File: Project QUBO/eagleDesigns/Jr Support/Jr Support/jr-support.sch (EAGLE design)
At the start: 195 parts, among them U1 PCA9685, U2 BME280

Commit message: 
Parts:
- removed 2PIN_2: 12V reg switch, molex:KK254_VERT_2PIN22-29-2021
- removed C64: (no value), resistor:C-USC0805
- removed C65, C80, C81: 22u, resistor:C-USC0805
- removed C66, C67: 2.2u, resistor:C-USC0805
- removed C69: 1u, resistor:C-USC0805
- removed C70, C76, C77, C78, C79, C82, C83: 0.1u, resistor:C-USC0805
- removed C71, C74, C75: 1n, resistor:C-USC0805
- removed C72, C73: 47n, resistor:C-USC0805
- removed C84: 100u,<50mO, resistor:C-USC0805
- removed D1: (no value), diode:DIODE-SOD123
- removed JP2, JP3: SUPERSABRE_2CIRCUIT, molex:SUPERSABRE_2CIRCUIT
- removed R26: 10\, resistor:R-US_R0805
- removed R27: 200k, resistor:R-US_R0805
- removed R28: 8.2k, resistor:R-US_R0805
- removed R29, R34: 100m, resistor:R-US_R0805
- removed R30, R31: ~50k, resistor:R-US_R0805
- removed R32: 10k, resistor:R-US_R0805
- removed R33, R35, R36: 22m, resistor:R-US_R0805
- added 2PIN_5: (no value), molex:KK254_VERT_2PIN22-29-2021
- added C33: 0.1u, resistor:C-USC0805
- added R13: 0, resistor:R-US_R0805
- added U$41, U$59: VTVS, diode:VTVS
- added U$42, U$43, U$44: ADC121C021, texas:ADC121C021
- added U$45: 74LVC1G14, NXP:74LVC1G14
- added U$57: NCP1117, ONSemi:NCP1117
- 2PIN_3: value Relay switch -> (none)
- C10, C16: value 47n -> (none)
- C13, C21, C7: value 0.1u -> (none)
- C14, C22, C8: value 47n -> 0.1u
- C15, C9: value 0.1u -> 47n
- C29: value 100u -> 47n; device resistor:CPOL-USE3.5-8 -> resistor:C-USC0805
- C30: value 100u -> (none); device resistor:CPOL-USE3.5-8 -> resistor:C-USC0805
- C32, C60: value (none) -> 1u
- C34, C61: value (none) -> 10u
- C37: value 10u -> 47n
- C56: value (none) -> 0.1u
- C57: value (none) -> 47n
- C59: value (none) -> 100u; device resistor:C-USC0805 -> resistor:CPOL-USE3.5-8
- C63: value 0.1u -> 10u
- JP1: value SUPERSABRE_2CIRCUIT -> 2_SUPERSABRE; device molex:SUPERSABRE_2CIRCUIT -> molex:2_SUPERSABRE
- R18: value 10k -> 510
- R20, R22: value 10k -> 0
- R21: value 12k -> 6.8k
- R23: value 51k -> 510
- R24: value 5.1k -> 6.8k
- R25: value 5m -> 100
- U$10, U$16: value 4A Fuse -> VTVS; device littelfuse:154-OMNI_BLOK -> diode:VTVS
- U$13, U$22: value ACS713SOIC -> VTVS; device allegro:ACS713SOIC -> diode:VTVS
- U$14, U$23, U$8: value 4A Fuse -> ACS713SOIC; device littelfuse:154-OMNI_BLOK -> allegro:ACS713SOIC
- U$15, U$9: value ACS713SOIC -> 4A Fuse; device allegro:ACS713SOIC -> littelfuse:154-OMNI_BLOK
- U$26: value 24V -> VTVS; device ONSemi:2-PIN_TVS_SOD-323 -> diode:VTVS
- U$27: value LTC4364MSOP -> 4A Fuse; device linear:LTC4364MSOP -> littelfuse:154-OMNI_BLOK
- U$28, U$32, U$34: value (none) -> VTVS; device fairchild:FDMC8360LET40PWR33 -> diode:VTVS
- U$29: value 24V -> ACS713SOIC; device diode:2-PIN_TVS_SOD-323 -> allegro:ACS713SOIC
- U$30, U$31, U$58: value 24V -> VTVS; device diode:2-PIN_TVS_SOD-323 -> diode:VTVS
- U$33: value MAX1737 -> VTVS; device maxim:MAX1737 -> diode:VTVS
- U$37: value (none) -> 4A Fuse; device fairchild:FDMC8360LET40PWR33 -> littelfuse:154-OMNI_BLOK
- U$38: value (none) -> VTVS; device resistor:DUAL-L -> diode:VTVS
- U$39: value SBR2065 -> ACS713SOIC; device diode:SBR2065 -> allegro:ACS713SOIC
- U$40: value NTCLE201E3 -> 4A Fuse; device vishay:NTCLE201E3 -> littelfuse:154-OMNI_BLOK
- U$46: value 5V -> ESD9X3; device ONSemi:2-PIN_TVS_SOD-323 -> diode:ESD9X3
- U$47: value 24V -> ESD9X3; device ONSemi:2-PIN_TVS_SOD-323 -> diode:ESD9X3
- U$48, U$49: value 12V -> ESD9X3; device ONSemi:2-PIN_TVS_SOD-323 -> diode:ESD9X3
- U$50: value 5V -> VTVS; device ONSemi:2-PIN_TVS_SOD-923 -> diode:VTVS
- U$51: value 3V3 -> DESD; device ONSemi:2-PIN_TVS_SOD-923 -> diode:DESD
- U$52, U$54: value 5V -> DESD; device ONSemi:2-PIN_TVS_SOD-923 -> diode:DESD
- U$53: value 12V -> DESD; device ONSemi:2-PIN_TVS_SOD-323 -> diode:DESD
- U$55: value 24V -> NCP1117; device diode:2-PIN_TVS_SOD-323 -> ONSemi:NCP1117
- U$56: value 24V -> 74LVC1G14; device diode:2-PIN_TVS_SOD-323 -> NXP:74LVC1G14
- U$7: value ACS713SOIC -> ADS7828; device allegro:ACS713SOIC -> texas:ADS7828
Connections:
- removed net N$18 (its old number): C10.1, U$9.FILTER
- removed net N$20 (its old number): U$10.P$1, U$9.IP-
- removed net N$25 (its old number): 4PIN_5.P$4, C58.1, U$14.P$2
- removed net N$27 (its old number): C16.1, U$15.FILTER
- removed net N$64: C70.1, R32.1
- removed net N$65: C66.1, C67.1, U$33.!SHDN!, U$33.CELL, U$33.VL
- removed net N$67: C71.1, R32.2, U$33.CCV
- removed net N$68: C69.1, R30.1, U$33.ISETIN, U$33.ISETOUT, U$33.REF
- removed net N$69: C72.1, U$33.CCI
- removed net N$70: C73.1, U$33.CCS
- removed net N$71: C74.1, U$33.TIMER1
- removed net N$72: C75.1, U$33.TIMER2
- removed net N$73: C76.1, R33.2, R35.2, R36.2, U$33.CSSP
- removed net N$74: C77.1, C80.1, C81.1, R33.1, R35.1, R36.1, U$33.CSSN, U$34.DRAIN
- removed net N$75: C78.1, U$33.LX
- removed net N$76: C78.2, D1.C, U$33.BST
- removed net N$77: C82.1, R29.2, R34.2, U$33.CS, U$38.P$3
- removed net N$79: U$33.DLO, U$37.GATE
- removed net N$80: U$33.DHI, U$34.GATE
- removed net N$81: U$34.SOURCE, U$37.DRAIN, U$38.P$1
- removed net N$82: U$33.PGND, U$37.SOURCE
- removed net N$83: C79.1, D1.A, U$33.VLO
- removed net N$84: U$33.THM, U$40.1
- removed net V_BATT: 2PIN_3.P$1, C65.1, R25.2, R28.2, U$27.OUT
- removed net V_BATT2: C29.+, C37.1, JP2.P$2, U$30.P$2
- removed net V_SHORE: C30.+, C62.1, JP3.P$2, U$29.P$2, U$39.A
- new net N$21: C15.1, U$14.FILTER
- new net N$23: R22.1, U$7.COM
- new net N$30: U$23.IP-, U$27.P$1
- new net N$49: C60.1, R23.2, U$56.IN
- new net T1_CURR: U$4.VIOUT, U$7.CH0
- new net T2_CURR: U$7.CH1, U$8.VIOUT
- new net T3_CURR: U$11.VIOUT, U$7.CH2
- new net T4_CURR: U$14.VIOUT, U$7.CH3
- new net T5_CURR: U$17.VIOUT, U$7.CH4
- new net T6_CURR: U$23.VIOUT, U$7.CH5
- new net T7_CURR: U$29.VIOUT, U$7.CH6
- new net T8_CURR: U$39.VIOUT, U$7.CH7
- net 12V: now also U$46.C, U$47.C, U$48.C, U$49.C; no longer U$48.P$2, U$49.P$2
- net 3V3: now also U2.SDO/ADR; no longer U$51.P$2
- net 5V: now also C14.1, C22.1, C33.1, C56.1, C8.1, R21.2, U$14.VCC, U$23.VCC, U$29.VCC, U$39.VCC, U$42.ADR1, U$42.VDD, U$43.ADR0, U$43.ADR1, U$43.VDD, U$44.VDD, U$45.VDD, U$51.C, U$52.C, U$53.C, U$54.C, U$7.REF, U$7.VDD, U$8.VCC; no longer 2PIN_2.P$1, C13.1, C15.1, C21.1, C9.1, U$13.VCC, U$15.VCC, U$22.VCC, U$46.P$2, U$50.P$2, U$52.P$2, U$7.VCC, U$9.VCC
- net AIN0: no longer U$19.VIOUT
- net AIN1: no longer U$2.VIOUT, U$35.VIOUT
- net AIN10: no longer U$17.VIOUT
- net AIN11: no longer U$22.VIOUT
- net AIN2: no longer U$4.VIOUT
- net AIN3: no longer U$7.VIOUT
- net AIN4: no longer U$9.VIOUT
- net AIN5: no longer U$11.VIOUT
- net AIN8: no longer U$13.VIOUT
- net AIN9: no longer U$15.VIOUT
- net CPU_ON: now also U$45.OUT; no longer 2PIN_2.P$2, C34.1, U$55.P$2
- net GND: now also C29.2, C30.2, C33.2, C59.-, R13.1, R22.2, U$10.A, U$13.A, U$14.GND, U$16.A, U$22.A, U$23.GND, U$26.A, U$28.A, U$29.GND, U$30.A, U$31.A, U$32.A, U$33.A, U$34.A, U$38.A, U$39.GND, U$41.A, U$42.ADR0, U$42.GND, U$43.GND, U$44.ADR0, U$44.ADR1, U$44.GND, U$46.A, U$47.A, U$48.A, U$49.A, U$50.A, U$51.A, U$52.A, U$53.A, U$54.A, U$55.GND, U$57.GND, U$7.A0, U$7.A1, U$8.GND; no longer C29.-, C30.-, C32.2, C59.2, C60.2, C64.2, C65.2, C66.2, C67.2, C69.2, C70.2, C71.2, C72.2, C73.2, C74.2, C75.2, C76.2, C77.2, C79.2, C80.2, C81.2, C82.2, C83.2, C84.2, JP2.P$1, JP3.P$1, R18.1, R22.1, R24.1, R31.1, U$13.GND, U$15.GND, U$22.GND, U$26.P$1, U$27.GND, U$29.P$1, U$30.P$1, U$31.P$1, U$33.GND, U$40.2, U$46.P$1, U$47.P$1, U$48.P$1, U$49.P$1, U$50.P$1, U$51.P$1, U$52.P$1, U$53.P$1, U$54.P$1, U$55.P$1, U$56.P$1, U$58.P$1, U$9.GND, U2.SDO/ADR
- net N$12: now also C9.1, U$8.FILTER; no longer C8.1, U$7.FILTER
- net N$14: now also U$31.C
- net N$16: now also C10.1, U$30.C, U$9.P$2; no longer C55.1, U$8.P$2
- net N$17: now also U$8.IP-, U$9.P$1; no longer U$7.IP-, U$8.P$1
- net N$19: now also C13.1, U$12.P$2, U$26.C; no longer C57.1, U$10.P$2
- net N$22: now also C16.1, U$15.P$2, U$28.C; no longer C56.1, U$12.P$2
- net N$24: now also U$14.IP-, U$15.P$1; no longer C14.1, U$13.FILTER
- net N$26: now also 4PIN_5.P$4, C21.1, U$18.P$2; no longer U$13.IP-, U$14.P$1
- net N$28: now also C29.1, U$23.FILTER; no longer 4PIN_6.P$4, C59.1, U$16.P$2
- net N$29: now also 4PIN_6.P$4, C30.1, U$13.C, U$27.P$2; no longer U$15.IP-, U$16.P$1
- net N$31: now also C37.1, U$29.FILTER; no longer 4PIN_7.P$4, C61.1, U$18.P$2
- net N$36: now also 4PIN_7.P$4, C55.1, U$16.C, U$37.P$2; no longer C22.1, U$22.FILTER
- net N$37: now also U$29.IP-, U$37.P$1; no longer R26.1, U$27.HGATE
- net N$38: now also C57.1, U$39.FILTER; no longer 4PIN_10.P$4, C60.1, U$23.P$2
- net N$39: now also 4PIN_10.P$4, C58.1, U$10.C, U$40.P$2; no longer R20.1, R21.2, U$27.UV
- net N$47: now also U$39.IP-, U$40.P$1; no longer R21.1, R22.2, U$27.OV
- net N$48: now also 2PIN_5.P$2, C60.2, U$56.GND, U$58.A; no longer U$22.IP-, U$23.P$1
- net N$50: now also 2PIN_5.P$1, R24.1, U$58.C; no longer R24.2, U$27.FB
- net N$51: now also 2PIN_3.P$2, C32.2, U$45.GND, U$59.A; no longer R20.2, R27.1
- net N$53: now also U$43.VIN; no longer C64.1, U$27.TMR
- net N$54: now also C62.1, R24.2, U$56.VDD, U$57.VOUT; no longer U$27.SOURCE, U$28.SOURCE, U$32.SOURCE
- net N$57: now also U$2.VIOUT, U$42.VIN; no longer R23.2, R28.1
- net N$58: no longer U$53.P$2
- net N$59: now also C32.1, R18.2, U$45.IN; no longer R26.2, U$28.GATE
- net N$60: now also U$44.VIN; no longer R25.1, U$27.SENSE, U$32.DRAIN
- net N$61: now also 2PIN_3.P$1, R18.1, R21.1, U$59.C; no longer U$27.DGATE, U$32.GATE
- net N$62: now also C63.1, R25.1, U$55.VOUT; no longer R30.2, R31.2, U$33.VADJ
- net N$63: now also R25.2, U$1.!INHIBIT!; no longer C63.1, U$33.DCIN, U$39.C
- net N$8: no longer U$54.P$2
- net RELAY-BATT: now also R20.2
- net RELAY-SHORE: now also R13.2
- net RELAY_CTRL: now also U$56.OUT; no longer 2PIN_3.P$2, C32.1, R18.2, U$56.P$2
- net RELAY_OUT: now also C34.1, C59.+, U$50.C, U$55.VIN; no longer U$58.P$2
- net SCL1: now also U$42.SCL, U$43.SCL, U$44.SCL, U$7.SCL
- net SDA1: now also U$42.SDA, U$43.SDA, U$44.SDA, U$7.SDA
- net V_BATT1: now also C61.1, R20.1, U$41.C, U$57.VIN; no longer C83.1, C84.1, R27.2, R29.1, R34.1, U$27.!SHDN!, U$27.VCC, U$28.DRAIN, U$31.P$2, U$33.BATT
- net V_THRUST: now also U$14.IP+, U$23.IP+, U$29.IP+, U$32.C, U$33.C, U$34.C, U$38.C, U$39.IP+, U$8.IP+; no longer U$13.IP+, U$15.IP+, U$22.IP+, U$26.P$2, U$47.P$2, U$7.IP+, U$9.IP+
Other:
- note added: "Address: 1001000 (Thrust ADC)"
- note added: "Address: 1010101 (12V ADC)"
- note added: "Address: 1011001 (5V ADC)"
- note added: "Address: 1011010 (VIN ADC)"
- note added: "Address: 1110111 (0x77) )(BAR30)"
- note added: "Address: 1110111 (0x77)(BME)"
- moved on the sheet: 2PIN_3, 4PIN_10, 4PIN_2, 4PIN_3, 4PIN_4, 4PIN_5, 4PIN_6, 4PIN_7, 5V_REG, C10, C11, C12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

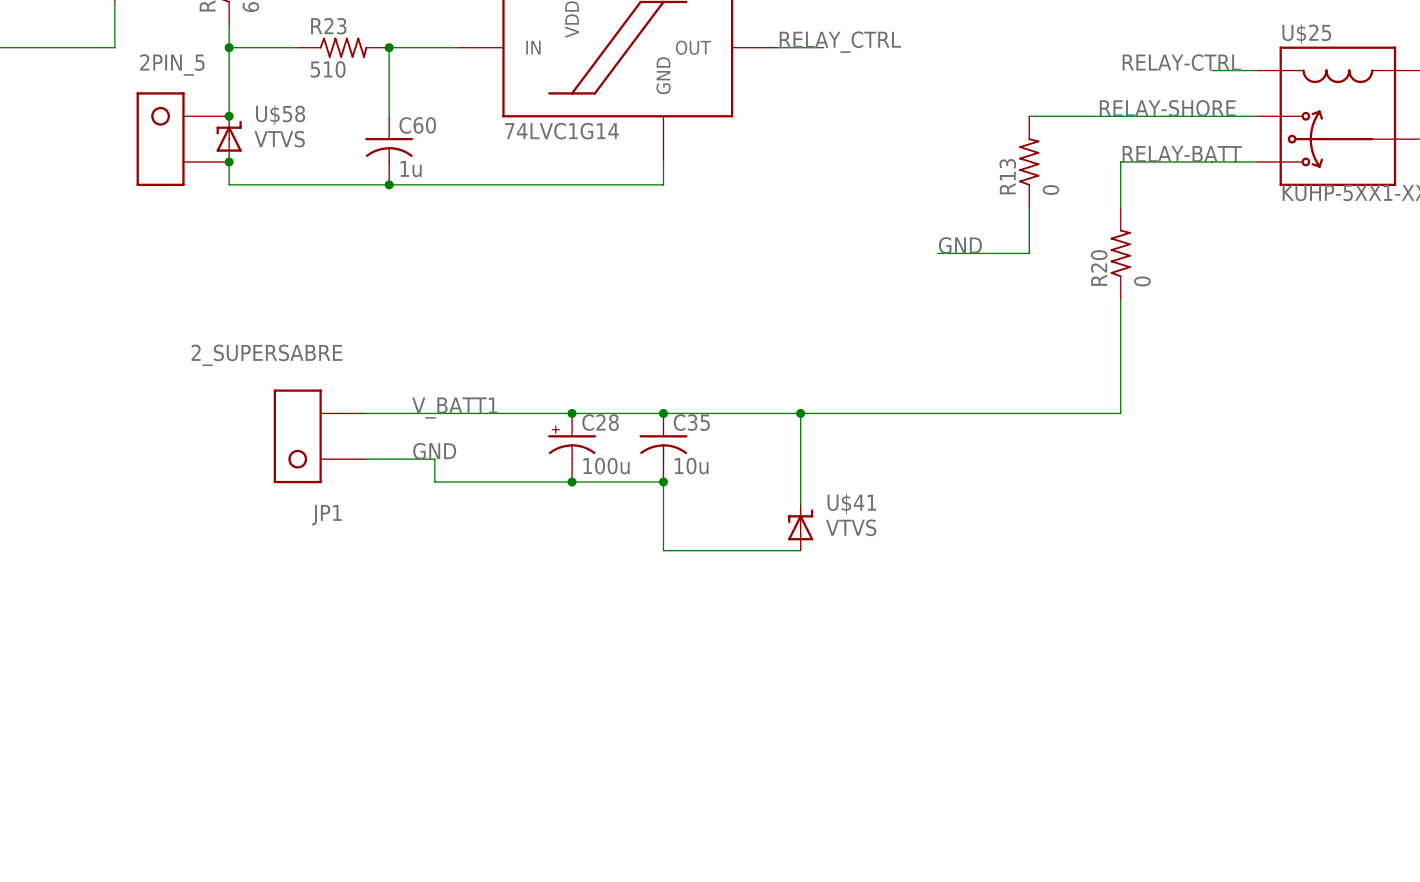
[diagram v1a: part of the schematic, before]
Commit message: 
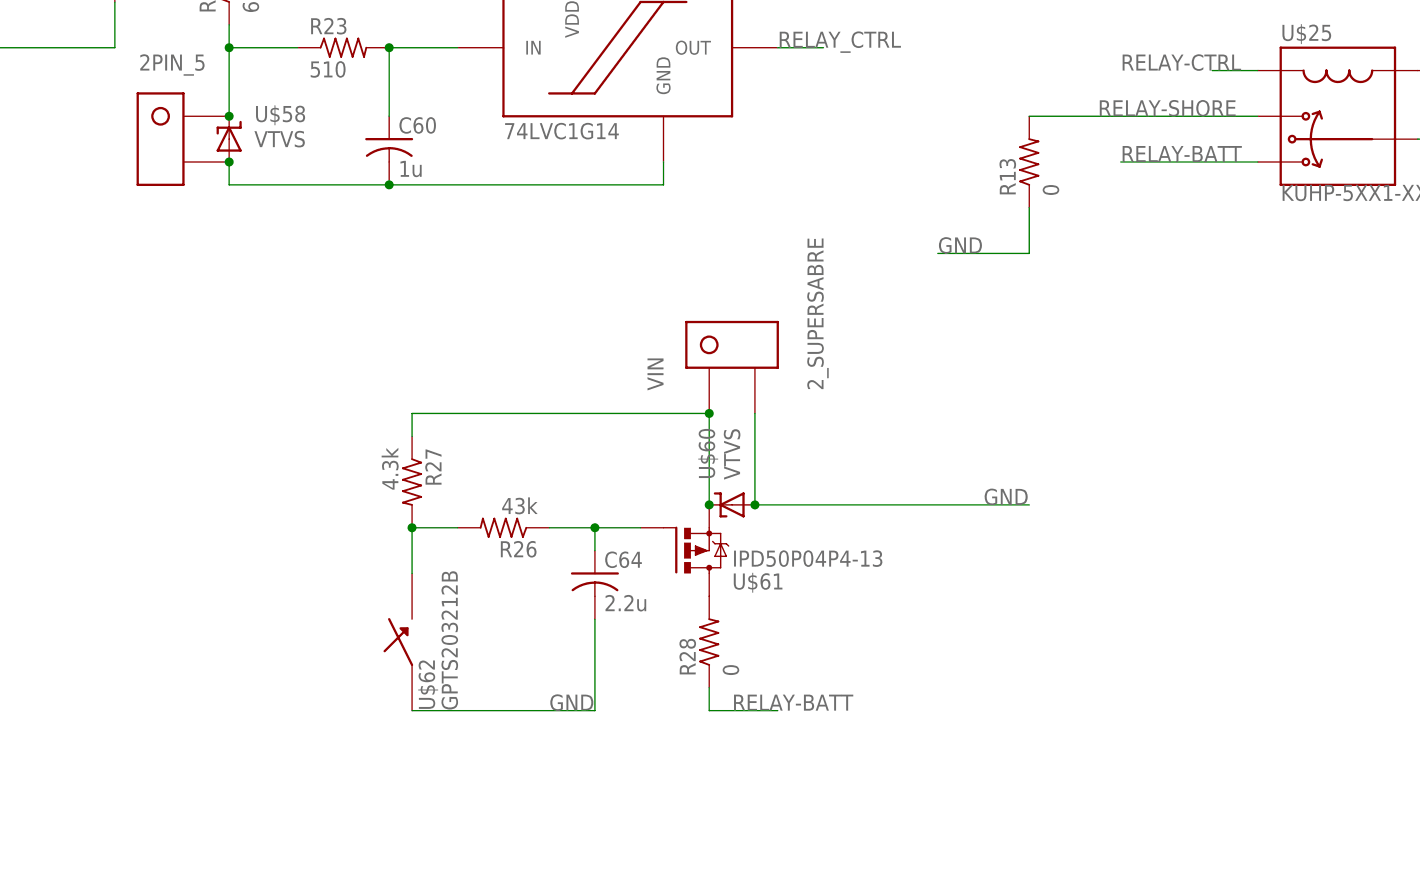
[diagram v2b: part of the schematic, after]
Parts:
- removed C28: 100u, resistor:CPOL-USE3.5-8
- removed C35: 10u, resistor:C-USC0805
- removed JP1: 2_SUPERSABRE, molex:2_SUPERSABRE
- removed R20: 0, resistor:R-US_R0805
- removed U$41: VTVS, diode:VTVS
- added C64: 2.2u, resistor:C-USC0805
- added R26: 43k, resistor:R-US_R0805
- added R27: 4.3k, resistor:R-US_R0805
- added R28: 0, resistor:R-US_R0805
- added U$60: VTVS, diode:VTVS
- added U$61: IPD50P04P4-13, transistor-power:IPD50P04P4-13
- added U$62: GPTS203212B, switches:GPTS203212B
- added VIN: 2_SUPERSABRE, molex:2_SUPERSABRE
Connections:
- new net N$64: R27.1, U$60.C, U$61.D, VIN.P$1
- new net N$65: C64.1, R26.1, U$61.G
- new net N$66: R26.2, R27.2, U$62.P$2
- new net N$67: R28.2, U$61.S
- net GND: now also C64.2, U$60.A, U$62.P$1, VIN.P$2; no longer C28.-, C35.2, JP1.P$1, U$41.A
- net RELAY-BATT: now also R28.1; no longer R20.2
- net V_BATT1: no longer C28.+, C35.1, JP1.P$2, R20.1, U$41.C
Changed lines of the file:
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@@
 <part name="U$1" library="texas" deviceset="PTN78060W" device=""/>
 <part name="U$2" library="allegro" deviceset="ACS713" device="SOIC"/>
-<part name="JP1" library="molex" deviceset="2_SUPERSABRE" device=""/>
 <part name="C2" library="resistor" deviceset="C-US" device="C0805" value="0.1u"/>
 <part name="C3" library="resistor" deviceset="C-US" device="C0805" value="47n"/>
@@
 <part name="R19" library="resistor" deviceset="R-US_" device="R0805" value="10k"/>
 <part name="C27" library="resistor" deviceset="CPOL-US" device="E3.5-8" value="100u"/>
-<part name="C28" library="resistor" deviceset="CPOL-US" device="E3.5-8" value="100u"/>
-<part name="C35" library="resistor" deviceset="C-US" device="C0805" value="10u"/>
 <part name="R13" library="resistor" deviceset="R-US_" device="R0805" value="0"/>
-<part name="R20" library="resistor" deviceset="R-US_" device="R0805" value="0"/>
 <part name="U$7" library="texas" deviceset="ADS7828" device=""/>
 <part name="R22" library="resistor" deviceset="R-US_" device="R0805" value="0"/>
@@
 <part name="U$34" library="diode" deviceset="VTVS" device=""/>
 <part name="U$38" library="diode" deviceset="VTVS" device=""/>
-<part name="U$41" library="diode" deviceset="VTVS" device=""/>
 <part name="U$46" library="diode" deviceset="ESD9X3" device=""/>
 <part name="U$47" library="diode" deviceset="ESD9X3" device=""/>
@@
 <part name="C63" library="resistor" deviceset="C-US" device="C0805" value="10u"/>
 <part name="R25" library="resistor" deviceset="R-US_" device="R0805" value="100"/>
+<part name="VIN" library="molex" deviceset="2_SUPERSABRE" device=""/>
+<part name="U$60" library="diode" deviceset="VTVS" device=""/>
+<part name="U$61" library="transistor-power" deviceset="IPD50P04P4-13" device=""/>
+<part name="R26" library="resistor" deviceset="R-US_" device="R0805" value="43k"/>
+<part name="C64" library="resistor" deviceset="C-US" device="C0805" value="2.2u"/>
+<part name="U$62" library="switches" deviceset="GPTS203212B" device=""/>
+<part name="R27" library="resistor" deviceset="R-US_" device="R0805" value="4.3k"/>
+<part name="R28" library="resistor" deviceset="R-US_" device="R0805" value="0"/>
 </parts>
 <sheets>
@@
 <instance part="U$1" gate="G$1" x="-152.4" y="-7.62"/>
 <instance part="U$2" gate="G$1" x="-66.04" y="-7.62"/>
-<instance part="JP1" gate="G$1" x="-388.62" y="40.64" rot="R180"/>
 <instance part="C2" gate="G$1" x="-45.72" y="5.08"/>
 <instance part="C3" gate="G$1" x="-35.56" y="-12.7"/>
@@
 <instance part="R19" gate="G$1" x="-259.08" y="81.28"/>
 <instance part="C27" gate="G$1" x="-127" y="144.78"/>
-<instance part="C28" gate="G$1" x="-358.14" y="40.64"/>
-<instance part="C35" gate="G$1" x="-347.98" y="40.64"/>
 <instance part="R13" gate="G$1" x="-307.34" y="71.12" rot="R90"/>
-<instance part="R20" gate="G$1" x="-297.18" y="60.96" rot="R90"/>
 <instance part="U$7" gate="G$1" x="58.42" y="-40.64"/>
 <instance part="R22" gate="G$1" x="45.72" y="-60.96" rot="R270"/>
@@
 <instance part="U$34" gate="G$1" x="73.66" y="261.62"/>
 <instance part="U$38" gate="G$1" x="-60.96" y="33.02"/>
-<instance part="U$41" gate="G$1" x="-332.74" y="30.48"/>
 <instance part="U$46" gate="G$1" x="304.8" y="193.04"/>
 <instance part="U$47" gate="G$1" x="284.48" y="203.2"/>
@@
 <instance part="C63" gate="G$1" x="-203.2" y="-25.4"/>
 <instance part="R25" gate="G$1" x="-185.42" y="-22.86"/>
+<instance part="VIN" gate="G$1" x="-340.36" y="50.8" rot="R90"/>
+<instance part="U$60" gate="G$1" x="-340.36" y="33.02" rot="R90"/>
+<instance part="U$61" gate="G$1" x="-345.44" y="27.94" rot="MR180"/>
+<instance part="R26" gate="G$1" x="-365.76" y="30.48" rot="R180"/>
+<instance part="C64" gate="G$1" x="-355.6" y="25.4"/>
+<instance part="U$62" gate="G$1" x="-375.92" y="17.78" rot="R90"/>
+<instance part="R27" gate="G$1" x="-375.92" y="35.56" rot="R270"/>
+<instance part="R28" gate="G$1" x="-342.9" y="17.78" rot="R90"/>
 </instances>
 <busses>
@@
 <wire x1="-167.64" y1="0" x2="-175.26" y2="0" width="0.1524" layer="91"/>
 <label x="-175.26" y="0" size="1.778" layer="95"/>
-</segment>
-<segment>
-<pinref part="JP1" gate="G$1" pin="P$1"/>
-<wire x1="-381" y1="38.1" x2="-373.38" y2="38.1" width="0.1524" layer="91"/>
-<label x="-375.92" y="38.1" size="1.778" layer="95"/>
-<pinref part="C28" gate="G$1" pin="-"/>
-<wire x1="-358.14" y1="35.56" x2="-373.38" y2="35.56" width="0.1524" layer="91"/>
-<wire x1="-373.38" y1="35.56" x2="-373.38" y2="38.1" width="0.1524" layer="91"/>
-<pinref part="C35" gate="G$1" pin="2"/>
-<wire x1="-347.98" y1="35.56" x2="-358.14" y2="35.56" width="0.1524" layer="91"/>
-<junction x="-358.14" y="35.56"/>
-<wire x1="-332.74" y1="27.94" x2="-347.98" y2="27.94" width="0.1524" layer="91"/>
-<wire x1="-347.98" y1="27.94" x2="-347.98" y2="35.56" width="0.1524" layer="91"/>
-<junction x="-347.98" y="35.56"/>
-<pinref part="U$41" gate="G$1" pin="A"/>
 </segment>
 <segment>
@@
 <label x="-220.98" y="-35.56" size="1.778" layer="95"/>
 </segment>
+<segment>
+<pinref part="VIN" gate="G$1" pin="P$2"/>
+<wire x1="-337.82" y1="43.18" x2="-337.82" y2="33.02" width="0.1524" layer="91"/>
+<wire x1="-337.82" y1="33.02" x2="-307.34" y2="33.02" width="0.1524" layer="91"/>
+<label x="-312.42" y="33.02" size="1.778" layer="95"/>
+<pinref part="U$60" gate="G$1" pin="A"/>
+<junction x="-337.82" y="33.02"/>
+</segment>
+<segment>
+<pinref part="U$62" gate="G$1" pin="P$1"/>
+<pinref part="C64" gate="G$1" pin="2"/>
+<wire x1="-375.92" y1="10.16" x2="-355.6" y2="10.16" width="0.1524" layer="91"/>
+<wire x1="-355.6" y1="10.16" x2="-355.6" y2="20.32" width="0.1524" layer="91"/>
+<label x="-360.68" y="10.16" size="1.778" layer="95"/>
+</segment>
 </net>
 <net name="5V-OUT" class="0">
@@
 <net name="V_BATT1" class="0">
 <segment>
-<pinref part="JP1" gate="G$1" pin="P$2"/>
-<label x="-375.92" y="43.18" size="1.778" layer="95"/>
-<pinref part="C28" gate="G$1" pin="+"/>
-<wire x1="-358.14" y1="43.18" x2="-381" y2="43.18" width="0.1524" layer="91"/>
-<pinref part="C35" gate="G$1" pin="1"/>
-<wire x1="-358.14" y1="43.18" x2="-347.98" y2="43.18" width="0.1524" layer="91"/>
-<junction x="-358.14" y="43.18"/>
-<junction x="-347.98" y="43.18"/>
-<pinref part="R20" gate="G$1" pin="1"/>
-<wire x1="-297.18" y1="55.88" x2="-297.18" y2="43.18" width="0.1524" layer="91"/>
-<wire x1="-297.18" y1="43.18" x2="-332.74" y2="43.18" width="0.1524" layer="91"/>
-<pinref part="U$41" gate="G$1" pin="C"/>
-<wire x1="-332.74" y1="43.18" x2="-347.98" y2="43.18" width="0.1524" layer="91"/>
-<wire x1="-332.74" y1="33.02" x2="-332.74" y2="43.18" width="0.1524" layer="91"/>
-<junction x="-332.74" y="43.18"/>
-</segment>
-<segment>
 <pinref part="C61" gate="G$1" pin="1"/>
 <pinref part="U$57" gate="G$1" pin="VIN"/>
@@
 <segment>
 <pinref part="U$25" gate="G$1" pin="5"/>
-<wire x1="-281.94" y1="71.12" x2="-284.48" y2="71.12" width="0.1524" layer="91"/>
 <label x="-297.18" y="71.12" size="1.778" layer="95"/>
-<pinref part="R20" gate="G$1" pin="2"/>
-<wire x1="-284.48" y1="71.12" x2="-287.02" y2="71.12" width="0.1524" layer="91"/>
-<wire x1="-297.18" y1="66.04" x2="-297.18" y2="71.12" width="0.1524" layer="91"/>
-<wire x1="-297.18" y1="71.12" x2="-287.02" y2="71.12" width="0.1524" layer="91"/>
+<wire x1="-297.18" y1="71.12" x2="-281.94" y2="71.12" width="0.1524" layer="91"/>
+</segment>
+<segment>
+<wire x1="-342.9" y1="10.16" x2="-335.28" y2="10.16" width="0.1524" layer="91"/>
+<label x="-340.36" y="10.16" size="1.778" layer="95"/>
+<pinref part="R28" gate="G$1" pin="1"/>
+<wire x1="-342.9" y1="10.16" x2="-342.9" y2="12.7" width="0.1524" layer="91"/>
 </segment>
 </net>
@@
 </segment>
 </net>
+<net name="N$64" class="0">
+<segment>
+<pinref part="VIN" gate="G$1" pin="P$1"/>
+<pinref part="U$60" gate="G$1" pin="C"/>
+<wire x1="-342.9" y1="43.18" x2="-342.9" y2="33.02" width="0.1524" layer="91"/>
+<pinref part="U$61" gate="G$1" pin="D"/>
+<junction x="-342.9" y="33.02"/>
+<pinref part="R27" gate="G$1" pin="1"/>
+<wire x1="-375.92" y1="40.64" x2="-375.92" y2="43.18" width="0.1524" layer="91"/>
+<wire x1="-375.92" y1="43.18" x2="-342.9" y2="43.18" width="0.1524" layer="91"/>
+<junction x="-342.9" y="43.18"/>
+</segment>
+</net>
+<net name="N$65" class="0">
+<segment>
+<pinref part="C64" gate="G$1" pin="1"/>
+<pinref part="R26" gate="G$1" pin="1"/>
+<wire x1="-355.6" y1="27.94" x2="-355.6" y2="30.48" width="0.1524" layer="91"/>
+<wire x1="-355.6" y1="30.48" x2="-360.68" y2="30.48" width="0.1524" layer="91"/>
+<pinref part="U$61" gate="G$1" pin="G"/>
+<wire x1="-355.6" y1="30.48" x2="-350.52" y2="30.48" width="0.1524" layer="91"/>
+<junction x="-355.6" y="30.48"/>
+</segment>
+</net>
+<net name="N$66" class="0">
+<segment>
+<pinref part="R26" gate="G$1" pin="2"/>
+<pinref part="U$62" gate="G$1" pin="P$2"/>
+<wire x1="-370.84" y1="30.48" x2="-375.92" y2="30.48" width="0.1524" layer="91"/>
+<wire x1="-375.92" y1="30.48" x2="-375.92" y2="25.4" width="0.1524" layer="91"/>
+<pinref part="R27" gate="G$1" pin="2"/>
+<junction x="-375.92" y="30.48"/>
+</segment>
+</net>
+<net name="N$67" class="0">
+<segment>
+<pinref part="U$61" gate="G$1" pin="S"/>
+<pinref part="R28" gate="G$1" pin="2"/>
+</segment>
+</net>
